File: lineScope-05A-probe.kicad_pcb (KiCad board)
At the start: 2 copper layers, 99.5 x 30 mm, 21 parts, among them J3 Conn_01x03, T1 TA1310-03

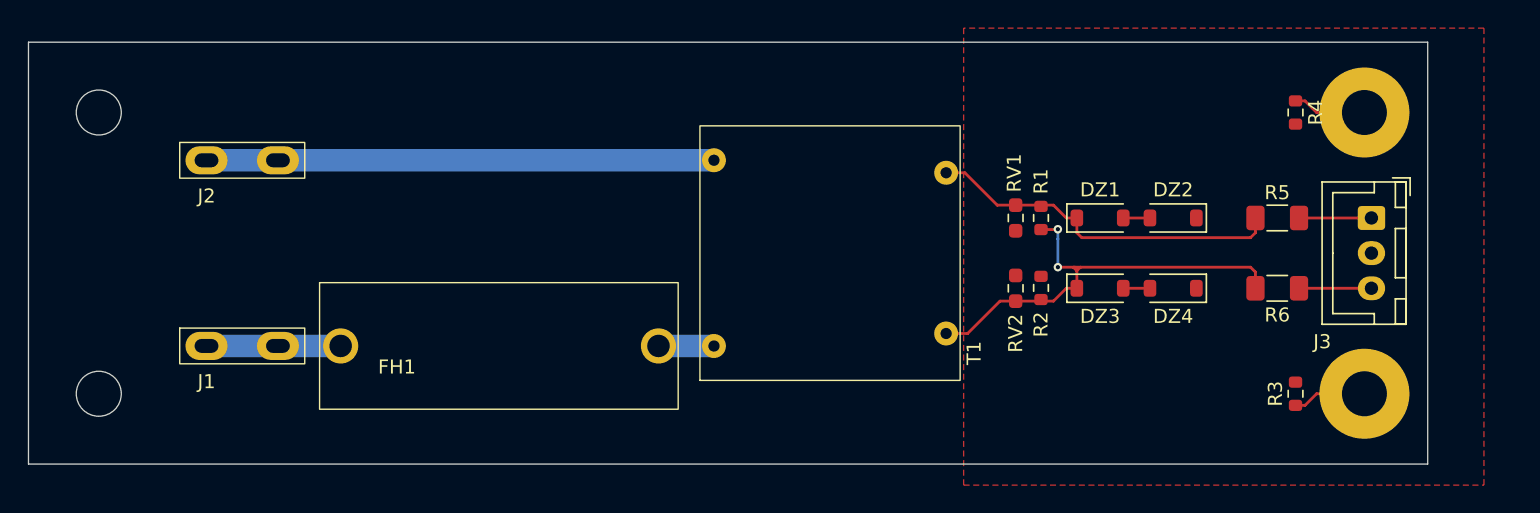
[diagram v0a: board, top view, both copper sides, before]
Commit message: Add passtrought connector
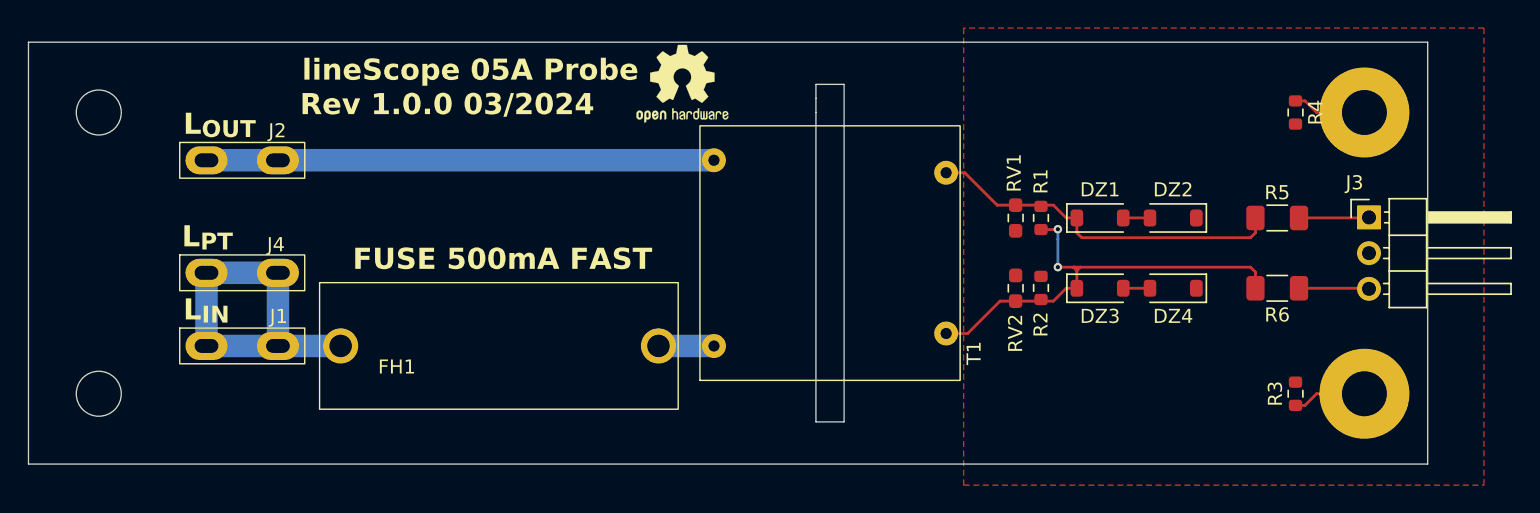
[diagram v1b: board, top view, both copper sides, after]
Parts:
- added J4: ~, Koszalix_Connectors_Tab:TE-1-726388-2, F.Cu at (99.2, 94.4)
- added REF**: OSHW-Logo2_7.3x6mm_SilkScreen, Symbol:OSHW-Logo2_7.3x6mm_SilkScreen, F.Cu at (130.5, 81.0)
- J3: footprint Connector_JST:JST_XH_B3B-XH-A_1x03_P2.50mm_Vertical -> Connector_PinHeader_2.54mm:PinHeader_1x03_P2.54mm_Horizontal
- moved J3 0.18 mm to (179.3, 90.5), turned to 0 degrees
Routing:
- net /HV_{L}: track 9.54 -> 25.0 mm
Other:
- outline, holes or cut-outs redrawn
- board text added: "FUSE 500mA FAST"
- board text added: "L_{IN}"
- board text added: "L_{OUT}"
- board text added: "L_{PT}"
- board text added: "Rev 1.0.0 03/2024"
- board text added: "lineScope 05A Probe"

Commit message: Minor fixes
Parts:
- added REF**: WEEE-Logo_4.2x6mm_SilkScreen, Symbol:WEEE-Logo_4.2x6mm_SilkScreen, F.Cu at (169.1, 103.7)
- added REF**: Attention, Koszalix_Symbols:Attention, F.Cu at (89.1, 86.1)
- J3: value Conn_01x03 -> ~; footprint Connector_PinHeader_2.54mm:PinHeader_1x03_P2.54mm_Horizontal -> Koszalix_Connectors_Tab:TE-1-726388-2
- J4: value ~ -> Conn_01x03; footprint Koszalix_Connectors_Tab:TE-1-726388-2 -> Connector_PinHeader_2.54mm:PinHeader_1x03_P2.54mm_Horizontal
- moved J3 80.2 mm to (99.2, 94.4)
- moved J4 80.2 mm to (179.3, 90.5)
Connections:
- J3 pad 1: Net-(J3-Pin_1) -> /HV_{L}
- J4 pad 1: /HV_{L} -> Net-(J4-Pin_1)
- R5 pad 2: Net-(J3-Pin_1) -> Net-(J4-Pin_1)
- R6 pad 2: Net-(J3-Pin_3) -> Net-(J4-Pin_3)
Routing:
- net Net-(J4-Pin_3): track 0.00 -> 5.15 mm
- net Net-(J4-Pin_1): track 0.00 -> 5.15 mm
- net Net-(J3-Pin_3): track 5.15 -> 0.00 mm
- net Net-(J3-Pin_1): track 5.15 -> 0.00 mm
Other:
- board text added: "0"
- board text added: "0 mm"
- board text added: "0,0000 mm / 0,0000 mm"
- board text added: "0,01 mm"
- board text added: "0,02"
- board text added: "0,035 mm"
- board text added: "0,3000 mm"
- board text added: "1"
- board text added: "1,51 mm"
- board text added: "1,6000 mm"
- board text added: "2"
- board text added: "3,3"
- board text added: "4,5"
- board text added: "99,5000 mm x 30,0000 mm"
- board text added: "B.Cu"
- board text added: "B.Mask"
- board text added: "B.Paste"
- board text added: "B.Silkscreen"
- board text added: "BOARD CHARACTERISTICS"
- board text added: "Board Thickness:"
- board text added: "Board overall dimensions:"
- board text added: "Bottom Silk Screen"
- board text added: "Bottom Solder Mask"
- board text added: "Bottom Solder Paste"
- board text added: "Castellated pads:"
- board text added: "Color"
- board text added: "Copper Finish:"
- board text added: "Copper Layer Count:"
- board text added: "Dielectric"
- board text added: "Edge card connectors:"
- board text added: "Epsilon R"
- board text added: "F.Cu"
- board text added: "F.Mask"
- board text added: "F.Paste"
- board text added: "F.Silkscreen"
- board text added: "FR4"
- board text added: "HIGH VOLTAGE"
- board text added: "Impedance Control:"
- board text added: "Layer Name"
- board text added: "Loss Tangent"
- board text added: "Material"
- board text added: "Min hole diameter:"
- board text added: "Min track/spacing:"
- board text added: "No"
- board text added: "None"
- board text added: "Not specified"
- board text added: "OUT+ GND OUT-"
- board text added: "Plated Board Edge:"
- board text added: "Thickness (mm)"
- board text added: "Top Silk Screen"
- board text added: "Top Solder Mask"
- board text added: "Top Solder Paste"
- board text added: "Type"
- board text added: "copper"
- board text added: "core"
